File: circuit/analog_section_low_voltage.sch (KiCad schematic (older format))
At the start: 38 parts, among them J2 Screw_Terminal_01x20, K1 Reed Relay DPST NC, Q2 2N2222 or similar, U11 LM7332, U12 LM7332_Power_Supply

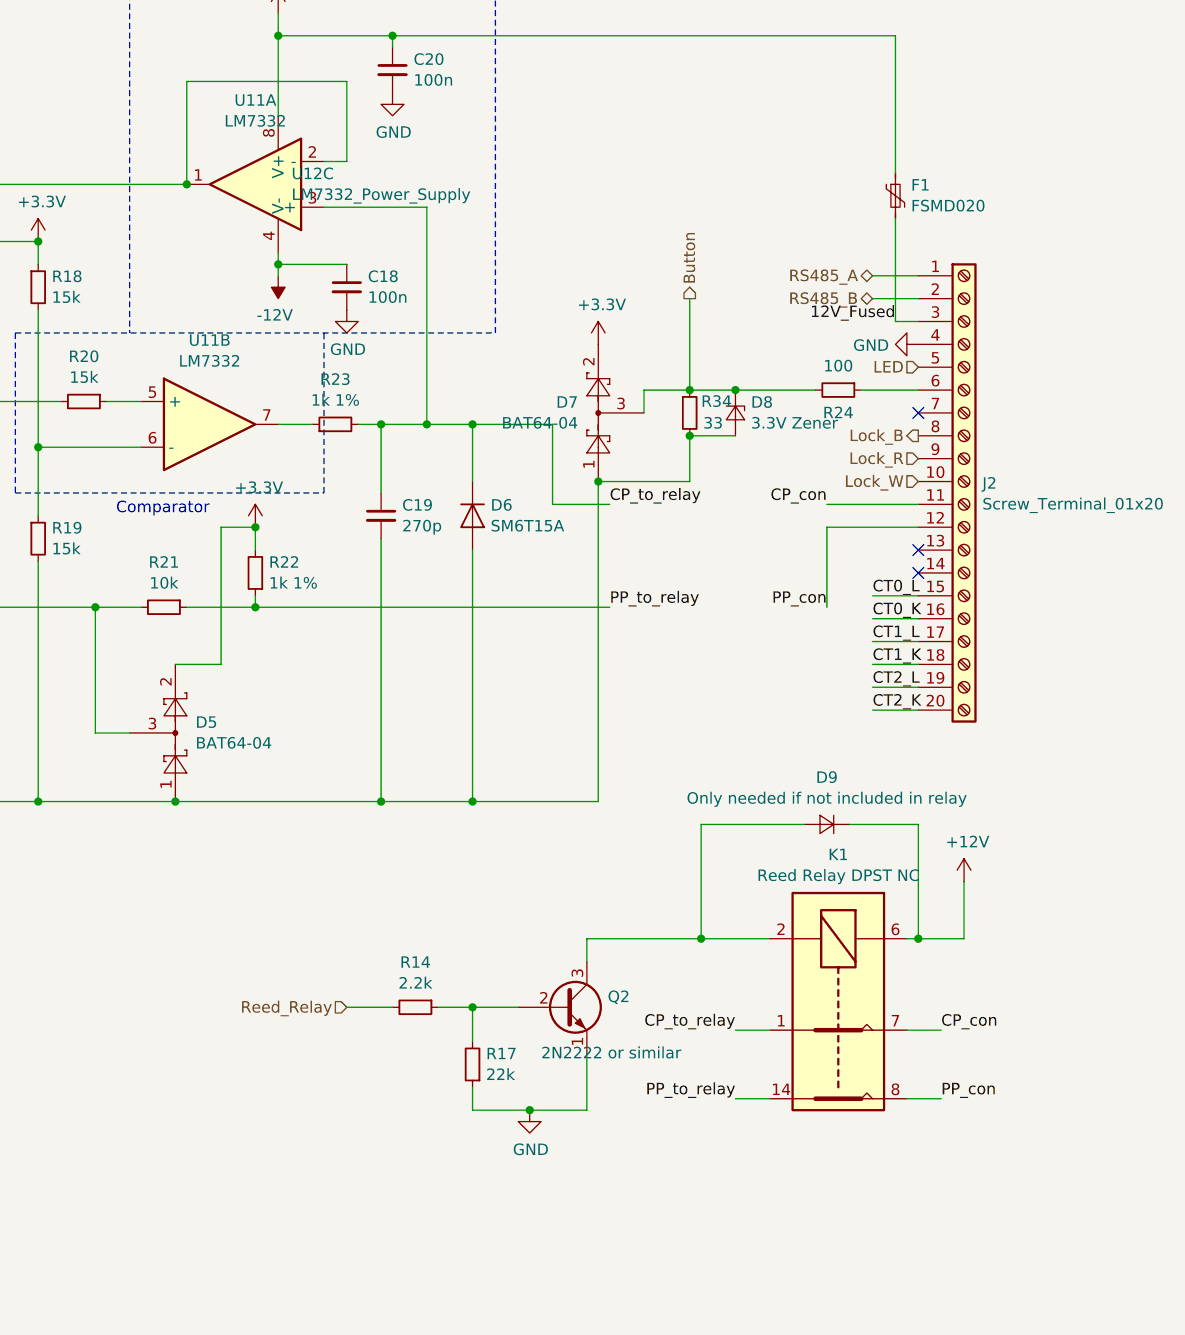
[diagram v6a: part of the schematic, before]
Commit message: Update Parts List with Mouser ordering info
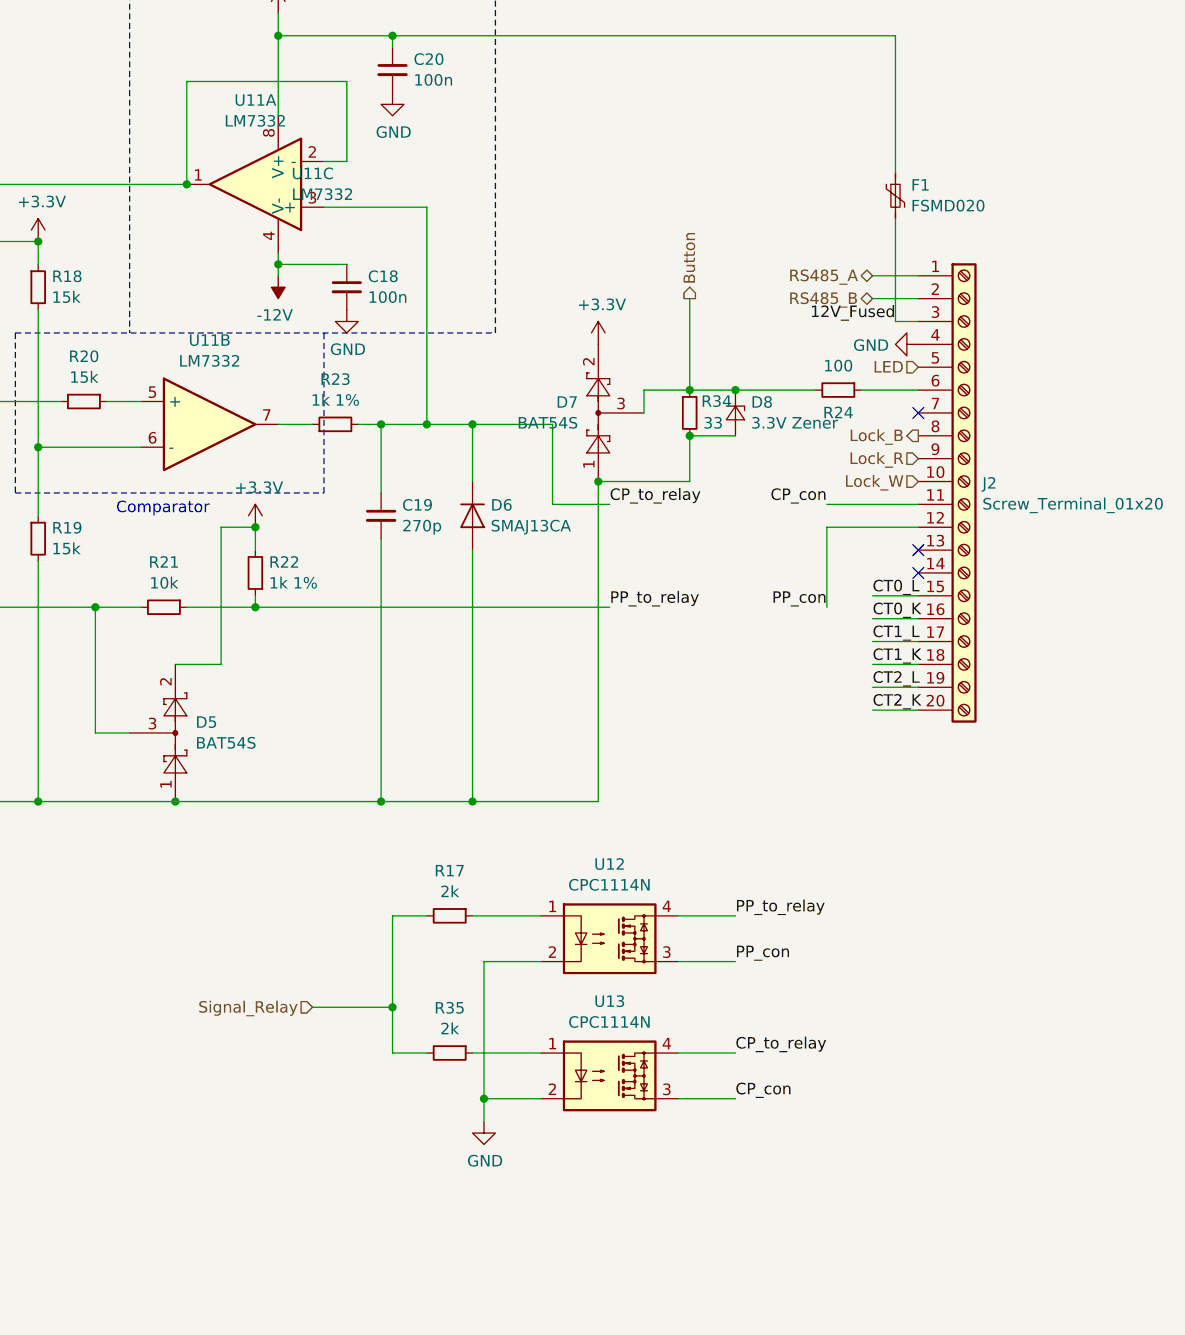
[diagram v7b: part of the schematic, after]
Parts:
- removed D9: Only needed if not included in relay, symbol Device:D_Small
- removed K1: Reed Relay DPST NC, symbol smartevse:Reed_Relay_DPST_NC
- removed Q2: 2N2222 or similar, symbol Transistor_BJT:2N3904
- removed R14: 2.2k, Resistor_SMD:R_0603_1608Metric_Pad1.05x0.95mm_HandSolder, symbol Device:R_Small
- added R35: 2k, Resistor_SMD:R_0603_1608Metric_Pad1.05x0.95mm_HandSolder, symbol Device:R_Small
- added U12, U13: CPC1114N, Package_SO:SOP-4_3.8x4.1mm_P2.54mm, symbol smartevse:CPC1114N
- C18, C20, C23, C24, C25: Part Kemet C0603C104K3RAC7867+ Keramik-Kondensator SMD 0603 100 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 -> (none); PartNo 1420339 -> (none); Supplier Conrad -> Mouser
- C19: Part Yageo CC0603JRNPO9BN271B Keramik-Kondensator SMD 0603 270 p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 -> (none); PartNo 445791 -> (none); Supplier Conrad -> Mouser
- D5, D7: value BAT64-04 -> BAT54S; Part Gleichrichter BAT64-04 (Dual) SOT-23-3 40 V Array - 1 Paar 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 -> (none); PartNo 152998 -> 583-BAT54S; Supplier Conrad -> Mouser
- D6: value SM6T15A -> SMAJ13CA; footprint Diode_SMD:D_SMB_Handsoldering -> Diode_SMD:D_SMA_Handsoldering; Part SM6T15A-E3/52 DO-214AA 14.3 V 600 W -> (none); PartNo 596320 -> 652-SMAJ13CA; Supplier Conrad -> Mouser
- D8: footprint Diode_SMD:D_MiniMELF_Handsoldering -> Diode_SMD:D_SOD-323_HandSoldering; Part TC-ZMM3.3 Gehäuseart (Halbleiter) SOD-80C Zener-Spannung 3.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 -> (none); PartNo 1581796 -> 833-MMXZ5226B-TP; Supplier Conrad -> Mouser
- F1: Part ESKA FSMD020 PTC-Sicherung -> (none); PartNo 524900 -> 576-1812L020PR; Supplier Conrad -> Mouser
- J2: PartNo (none) -> 651-1828206; Supplier (none) -> Mouser
- R13: Part Panasonic ERJ-6ENF4022V Dickschicht-Widerstand 40.2 kΩ SMD 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 -> (none); PartNo 1480312 -> 594-MCT06030C4022FP5; Supplier Conrad -> Mouser
- R15, R21, R26, R27: Part TRU COMPONENTS TC-0603SAF1002T5E203 Dickschicht-Widerstand 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 -> (none); PartNo 1585269 -> 594-MCT06030C1002FP5; Supplier Conrad -> Mouser
- R16, R18, R19, R20: Part TRU COMPONENTS TC-0603SAJ0153T5E203 Dickschicht-Widerstand 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 -> (none); PartNo 1585827 -> 594-MCT06030C1502FP5; Supplier Conrad -> Mouser
- R17: value 22k -> 2k; Part TRU COMPONENTS TC-HP03W5F2202T5E203 Dickschicht-Widerstand 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 -> (none); PartNo 1584163 -> 594-MCT06030C2001FP5; Supplier Conrad -> Mouser
- R22, R23: Part TRU COMPONENTS TC-HP03W5F1001T5E203 Dickschicht-Widerstand 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 -> (none); PartNo 1585508 -> 594-MCT06030C1001FP5; Supplier Conrad -> Mouser
- R24, R28, R29, R30: Part TRU COMPONENTS TC-0603SAJ0101T5E203 Dickschicht-Widerstand 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 -> (none); PartNo 1583838 -> 594-MCT06030C1000FP5; Supplier Conrad -> Mouser
- R31, R32, R33: Part TRU COMPONENTS TC-0603SAJ0220T5E203 Dickschicht-Widerstand 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 -> (none); PartNo 1585778 -> 594-MCT06030C2209FP5; Supplier Conrad -> Mouser
- R34: Part TRU COMPONENTS TC-0603SAJ0330T5E203 Dickschicht-Widerstand 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 -> (none); PartNo 1584262 -> 594-MCT06030C3309FP5; Supplier Conrad -> Mouser
- U11: footprint (none) -> Package_SO:SOIC-8_3.9x4.9mm_P1.27mm; Supplier (none) -> Mouser
- U11: renamed from U12; value LM7332_Power_Supply -> LM7332; footprint (none) -> Package_SO:SOIC-8_3.9x4.9mm_P1.27mm; Supplier (none) -> Mouser
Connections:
- net CP_con: now also U13.3
- net CP_to_relay: now also U13.4
- net GND: now also U12.2, U13.2; no longer R17.1
- net PP_con: now also U12.3
- net PP_to_relay: now also U12.4
- net Signal_Relay: now reaches R17.2
- net Signal_Relay: now also R35.2
- new net: R17.1, U12.1
- new net: R35.1, U13.1

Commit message: Finish schematic rev1 and footprint assignment
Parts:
- C18, C20, C23, C24, C25: footprint Capacitor_SMD:C_0603_1608Metric_Pad1.05x0.95mm_HandSolder -> Capacitor_SMD:C_0805_2012Metric_Pad1.15x1.40mm_HandSolder; PartNo (none) -> 963-EMF212B7104KGHT
- C19: footprint Capacitor_SMD:C_0603_1608Metric_Pad1.05x0.95mm_HandSolder -> Capacitor_SMD:C_0805_2012Metric_Pad1.15x1.40mm_HandSolder; PartNo (none) -> 77-VJ0805A271KXJPBC
- J2: value Screw_Terminal_01x20 -> Screw_Terminal_01x18; footprint (none) -> atmevse-footprints:CUI_TB004-508-18BE; symbol Connector:Screw_Terminal_01x20 -> Connector:Screw_Terminal_01x18; PartNo 651-1828206 -> 490-TB004-508-18BE
- U11: PartNo (none) -> 926-LM7332MA/NOPB
- U12, U13: PartNo (none) -> 849-CPC1114N
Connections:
- net BIAS: now also J2.14 (Pin_14); no longer J2.20 (Pin_20)
- net CT0_L: now also J2.13 (Pin_13); no longer J2.15 (Pin_15)
- net CT1_L: now also J2.15 (Pin_15); no longer J2.17 (Pin_17)
- net CT2_L: now also J2.17 (Pin_17); no longer J2.19 (Pin_19)
- no-connect marks 3 -> 1
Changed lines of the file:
@@
 Sheet 4 4
 Title ""
-Date "2020-05-29"
-Rev "0.7"
+Date "2020-06-01"
+Rev "1.0"
 Comp ""
 Comment1 "DONE: CT inputs on J2"
@@
 $EndDescr
 $Comp
-L Connector:Screw_Terminal_01x20 J2
+L Connector:Screw_Terminal_01x18 J2
 U 1 1 5E903CA7
-P 8700 3100
-F 0 "J2" H 8780 3092 50  0000 L CNN
-F 1 "Screw_Terminal_01x20" H 8780 3001 50  0000 L CNN
-F 2 "" H 8700 3100 50  0001 C CNN
-F 3 "https://www.mouser.de/datasheet/2/324/2/828206-1447938.pdf" H 8700 3100 50  0001 C CNN
-F 4 "Mouser" H 8700 3100 50  0001 C CNN "Supplier"
-F 5 "651-1828206 " H 8700 3100 50  0001 C CNN "PartNo"
-	1    8700 3100
+P 8700 3000
+F 0 "J2" H 8780 2992 50  0000 L CNN
+F 1 "Screw_Terminal_01x18" H 8780 2901 50  0000 L CNN
+F 2 "atmevse-footprints:CUI_TB004-508-18BE" H 8700 3000 50  0001 C CNN
+F 3 "https://www.mouser.de/datasheet/2/324/2/828206-1447938.pdf" H 8700 3000 50  0001 C CNN
+F 4 "Mouser" H 8700 3000 50  0001 C CNN "Supplier"
+F 5 "490-TB004-508-18BE" H 8700 3000 50  0001 C CNN "PartNo"
+	1    8700 3000
 	1    0    0    -1
 $EndComp
@@
 F 0 "C20" H 6292 1346 50  0000 L CNN
 F 1 "100n" H 6292 1255 50  0000 L CNN
-F 2 "Capacitor_SMD:C_0603_1608Metric_Pad1.05x0.95mm_HandSolder" H 6200 1300 50  0001 C CNN
+F 2 "Capacitor_SMD:C_0805_2012Metric_Pad1.15x1.40mm_HandSolder" H 6200 1300 50  0001 C CNN
 F 3 "~" H 6200 1300 50  0001 C CNN
 F 4 "" H 6200 1300 50  0001 C CNN "Part"
-F 5 "" H 6200 1300 50  0001 C CNN "PartNo"
+F 5 "963-EMF212B7104KGHT " H 6200 1300 50  0001 C CNN "PartNo"
 F 6 "Mouser" H 6200 1300 50  0001 C CNN "Supplier"
 	1    6200 1300
@@
 F 3 "http://www.ti.com/lit/ds/symlink/lm7332.pdf?HQS=TI-null-null-mousermode-df-pf-null-wwe&ts=1590747908099" H 5400 2850 50  0001 C CNN
 F 4 "Mouser" H 5400 2850 50  0001 C CNN "Supplier"
+F 5 "926-LM7332MA/NOPB" H 5400 2850 50  0001 C CNN "PartNo"
 	2    5400 2850
 	1    0    0    -1
@@
 F 3 "http://www.ti.com/lit/ds/symlink/lm7332.pdf?HQS=TI-null-null-mousermode-df-pf-null-wwe&ts=1590747908099" H 5800 1800 50  0001 C CNN
 F 4 "Mouser" H 5800 1800 50  0001 C CNN "Supplier"
+F 5 "926-LM7332MA/NOPB" H 5800 1800 50  0001 C CNN "PartNo"
 	3    5800 1800
 	1    0    0    -1
@@
 F 0 "C18" H 6092 2296 50  0000 L CNN
 F 1 "100n" H 6092 2205 50  0000 L CNN
-F 2 "Capacitor_SMD:C_0603_1608Metric_Pad1.05x0.95mm_HandSolder" H 6000 2250 50  0001 C CNN
+F 2 "Capacitor_SMD:C_0805_2012Metric_Pad1.15x1.40mm_HandSolder" H 6000 2250 50  0001 C CNN
 F 3 "~" H 6000 2250 50  0001 C CNN
 F 4 "" H 6000 2250 50  0001 C CNN "Part"
-F 5 "" H 6000 2250 50  0001 C CNN "PartNo"
+F 5 "963-EMF212B7104KGHT " H 6000 2250 50  0001 C CNN "PartNo"
 F 6 "Mouser" H 6000 2250 50  0001 C CNN "Supplier"
 	1    6000 2250
@@
 F 0 "C19" H 6242 3296 50  0000 L CNN
 F 1 "270p" H 6242 3205 50  0000 L CNN
-F 2 "Capacitor_SMD:C_0603_1608Metric_Pad1.05x0.95mm_HandSolder" H 6150 3250 50  0001 C CNN
+F 2 "Capacitor_SMD:C_0805_2012Metric_Pad1.15x1.40mm_HandSolder" H 6150 3250 50  0001 C CNN
 F 3 "~" H 6150 3250 50  0001 C CNN
 F 4 "" H 6150 3250 50  0001 C CNN "Part"
-F 5 "" H 6150 3250 50  0001 C CNN "PartNo"
+F 5 "77-VJ0805A271KXJPBC " H 6150 3250 50  0001 C CNN "PartNo"
 F 6 "Mouser" H 6150 3250 50  0001 C CNN "Supplier"
 	1    6150 3250
@@
 F 0 "C23" H 1392 5396 50  0000 L CNN
 F 1 "100n" H 1392 5305 50  0000 L CNN
-F 2 "Capacitor_SMD:C_0603_1608Metric_Pad1.05x0.95mm_HandSolder" H 1300 5350 50  0001 C CNN
+F 2 "Capacitor_SMD:C_0805_2012Metric_Pad1.15x1.40mm_HandSolder" H 1300 5350 50  0001 C CNN
 F 3 "~" H 1300 5350 50  0001 C CNN
 F 4 "" H 1300 5350 50  0001 C CNN "Part"
-F 5 "" H 1300 5350 50  0001 C CNN "PartNo"
+F 5 "963-EMF212B7104KGHT " H 1300 5350 50  0001 C CNN "PartNo"
 F 6 "Mouser" H 1300 5350 50  0001 C CNN "Supplier"
 	1    1300 5350
@@
 F 0 "C24" H 1392 6296 50  0000 L CNN
 F 1 "100n" H 1392 6205 50  0000 L CNN
-F 2 "Capacitor_SMD:C_0603_1608Metric_Pad1.05x0.95mm_HandSolder" H 1300 6250 50  0001 C CNN
+F 2 "Capacitor_SMD:C_0805_2012Metric_Pad1.15x1.40mm_HandSolder" H 1300 6250 50  0001 C CNN
 F 3 "~" H 1300 6250 50  0001 C CNN
 F 4 "" H 1300 6250 50  0001 C CNN "Part"
-F 5 "" H 1300 6250 50  0001 C CNN "PartNo"
+F 5 "963-EMF212B7104KGHT " H 1300 6250 50  0001 C CNN "PartNo"
 F 6 "Mouser" H 1300 6250 50  0001 C CNN "Supplier"
 	1    1300 6250
@@
 F 0 "C25" H 1392 7196 50  0000 L CNN
 F 1 "100n" H 1392 7105 50  0000 L CNN
-F 2 "Capacitor_SMD:C_0603_1608Metric_Pad1.05x0.95mm_HandSolder" H 1300 7150 50  0001 C CNN
+F 2 "Capacitor_SMD:C_0805_2012Metric_Pad1.15x1.40mm_HandSolder" H 1300 7150 50  0001 C CNN
 F 3 "~" H 1300 7150 50  0001 C CNN
 F 4 "" H 1300 7150 50  0001 C CNN "Part"
-F 5 "" H 1300 7150 50  0001 C CNN "PartNo"
+F 5 "963-EMF212B7104KGHT " H 1300 7150 50  0001 C CNN "PartNo"
 F 6 "Mouser" H 1300 7150 50  0001 C CNN "Supplier"
 	1    1300 7150
@@
 	8100 3300 8500 3300
 Wire Wire Line
+	8500 3400 8300 3400
+Wire Wire Line
+	8500 3500 8300 3500
+Wire Wire Line
 	8500 3600 8300 3600
 Wire Wire Line
@@
 Wire Wire Line
 	8500 3900 8300 3900
-Wire Wire Line
-	8500 4000 8300 4000
-Wire Wire Line
-	8500 4100 8300 4100
+Text Label 8300 3400 0    50   ~ 0
+CT0_L
+Text Label 8300 3500 0    50   ~ 0
+CT0_K
 Text Label 8300 3600 0    50   ~ 0
-CT0_L
+CT1_L
 Text Label 8300 3700 0    50   ~ 0
-CT0_K
+CT1_K
 Text Label 8300 3800 0    50   ~ 0
-CT1_L
+CT2_L
 Text Label 8300 3900 0    50   ~ 0
-CT1_K
-Text Label 8300 4000 0    50   ~ 0
-CT2_L
-Text Label 8300 4100 0    50   ~ 0
 CT2_K
 Wire Wire Line
@@
 Text Notes 850  4750 0    50   ~ 0
 VDD/2 Bias Voltage for CT input\n
-NoConn ~ 8500 3400
-NoConn ~ 8500 3500
 Wire Wire Line
 	6200 1150 8400 1150
@@
 F 3 "https://www.mouser.de/datasheet/2/240/CPC1114N-1548344.pdf" H 7100 5100 50  0001 L CNN
 F 4 "Mouser" H 7150 5100 50  0001 C CNN "Supplier"
+F 5 "849-CPC1114N" H 7150 5100 50  0001 C CNN "PartNo"
 	1    7150 5100
 	1    0    0    -1
@@
 F 3 "https://www.mouser.de/datasheet/2/240/CPC1114N-1548344.pdf" H 7100 5700 50  0001 L CNN
 F 4 "Mouser" H 7150 5700 50  0001 C CNN "Supplier"
+F 5 "849-CPC1114N" H 7150 5700 50  0001 C CNN "PartNo"
 	1    7150 5700
 	1    0    0    -1
@@
 F 3 "http://www.ti.com/lit/ds/symlink/lm7332.pdf?HQS=TI-null-null-mousermode-df-pf-null-wwe&ts=1590747908099" H 5600 1800 50  0001 C CNN
 F 4 "Mouser" H 5600 1800 50  0001 C CNN "Supplier"
+F 5 "926-LM7332MA/NOPB" H 5600 1800 50  0001 C CNN "PartNo"
 	1    5600 1800
 	-1   0    0    1
